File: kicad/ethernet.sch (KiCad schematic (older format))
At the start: 5 parts

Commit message: add ksz9021gn, cfps-73 to library
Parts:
- removed D? (x2): 88e1512, symbol 88e1512
- added D?: KSZ9021GN, symbol KSZ9021GN
- added D? (x3): 10cl025, symbol 10cl025
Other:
- moved on the sheet: D?, X?
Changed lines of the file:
@@
 LIBS:contrib
 LIBS:valves
-LIBS:88e1512
 LIBS:10cl025
 LIBS:l829-1j1t-43
 LIBS:nup4114upxv6t1g
+LIBS:ksz9021rl
+LIBS:ksz9021gn
+LIBS:cfps-73
+LIBS:fpgagigepi-cache
 EELAYER 25 0
 EELAYER END
@@
 encoding utf-8
 Sheet 3 4
-Title ""
-Date ""
-Rev ""
-Comp ""
-Comment1 ""
-Comment2 ""
+Title "figa-pi"
+Date "2018-04-13"
+Rev "1.0"
+Comp "GENERAL RND"
+Comment1 "07e20003"
+Comment2 "Y. Remizov"
 Comment3 ""
 Comment4 ""
@@
 L L829-1J1T-43 X?
 U 1 1 5AC780DA
-P 9200 2400
-F 0 "X?" H 8700 3250 60  0000 C CNN
-F 1 "L829-1J1T-43" H 9450 3250 60  0000 C CNN
-F 2 "" H 9200 2700 60  0001 C CNN
-F 3 "" H 9200 2700 60  0001 C CNN
-	1    9200 2400
-	1    0    0    -1
-$EndComp
-$Comp
-L 88e1512 D?
-U 1 1 5AC7812F
-P 5400 2500
-F 0 "D?" H 4500 3550 60  0000 C CNN
-F 1 "88e1512" H 5400 3100 60  0000 C CNN
-F 2 "" H 5350 2600 60  0001 C CNN
-F 3 "" H 5350 2600 60  0001 C CNN
-	1    5400 2500
-	1    0    0    -1
-$EndComp
-$Comp
-L 88e1512 D?
-U 2 1 5AC78188
-P 5350 5200
-F 0 "D?" H 4450 6250 60  0000 C CNN
-F 1 "88e1512" H 5350 5800 60  0000 C CNN
-F 2 "" H 5300 5300 60  0001 C CNN
-F 3 "" H 5300 5300 60  0001 C CNN
-	2    5350 5200
+P 9200 2300
+F 0 "X?" H 8700 3150 60  0000 C CNN
+F 1 "L829-1J1T-43" H 9450 3150 60  0000 C CNN
+F 2 "" H 9200 2600 60  0001 C CNN
+F 3 "" H 9200 2600 60  0001 C CNN
+	1    9200 2300
 	1    0    0    -1
 $EndComp
@@
 L NUP4114UPXV6T1G D?
 U 1 1 5AC781CD
-P 8800 4300
-F 0 "D?" H 8600 4600 60  0000 C CNN
-F 1 "NUP4114UPXV6T1G" H 8800 4000 60  0000 C CNN
-F 2 "" H 8800 4250 60  0001 C CNN
-F 3 "" H 8800 4250 60  0001 C CNN
-	1    8800 4300
+P 8850 4050
+F 0 "D?" H 8650 4350 60  0000 C CNN
+F 1 "NUP4114UPXV6T1G" H 8850 3750 60  0000 C CNN
+F 2 "" H 8850 4000 60  0001 C CNN
+F 3 "" H 8850 4000 60  0001 C CNN
+	1    8850 4050
 	1    0    0    -1
 $EndComp
@@
 L NUP4114UPXV6T1G D?
 U 1 1 5AC78238
-P 8800 5200
-F 0 "D?" H 8600 5500 60  0000 C CNN
-F 1 "NUP4114UPXV6T1G" H 8800 4900 60  0000 C CNN
-F 2 "" H 8800 5150 60  0001 C CNN
-F 3 "" H 8800 5150 60  0001 C CNN
-	1    8800 5200
+P 8850 4950
+F 0 "D?" H 8650 5250 60  0000 C CNN
+F 1 "NUP4114UPXV6T1G" H 8850 4650 60  0000 C CNN
+F 2 "" H 8850 4900 60  0001 C CNN
+F 3 "" H 8850 4900 60  0001 C CNN
+	1    8850 4950
 	1    0    0    -1
 $EndComp
+$Comp
+L KSZ9021GN D?
+U 1 1 5AD094DF
+P 5500 3100
+F 0 "D?" H 4950 4750 60  0000 C CNN
+F 1 "KSZ9021GN" H 5850 4750 60  0000 C CNN
+F 2 "" H 5250 4000 60  0001 C CNN
+F 3 "" H 5250 4000 60  0001 C CNN
+	1    5500 3100
+	1    0    0    -1
+$EndComp
+$Comp
+L 10cl025 D?
+U 4 1 5AD09564
+P 1550 2100
+F 0 "D?" H 1200 2750 60  0000 C CNN
+F 1 "10cl025" H 1800 2750 60  0000 C CNN
+F 2 "" H 550 2450 60  0001 C CNN
+F 3 "" H 550 2450 60  0001 C CNN
+	4    1550 2100
+	-1   0    0    -1
+$EndComp
+$Comp
+L 10cl025 D?
+U 7 1 5AD095B3
+P 1550 3600
+F 0 "D?" H 1200 4250 60  0000 C CNN
+F 1 "10cl025" H 1800 4250 60  0000 C CNN
+F 2 "" H 550 3950 60  0001 C CNN
+F 3 "" H 550 3950 60  0001 C CNN
+	7    1550 3600
+	-1   0    0    -1
+$EndComp
+$Comp
+L 10cl025 D?
+U 8 1 5AD09652
+P 1550 5000
+F 0 "D?" H 1200 5650 60  0000 C CNN
+F 1 "10cl025" H 1800 5650 60  0000 C CNN
+F 2 "" H 550 5350 60  0001 C CNN
+F 3 "" H 550 5350 60  0001 C CNN
+	8    1550 5000
+	-1   0    0    -1
+$EndComp
 $EndSCHEMATC

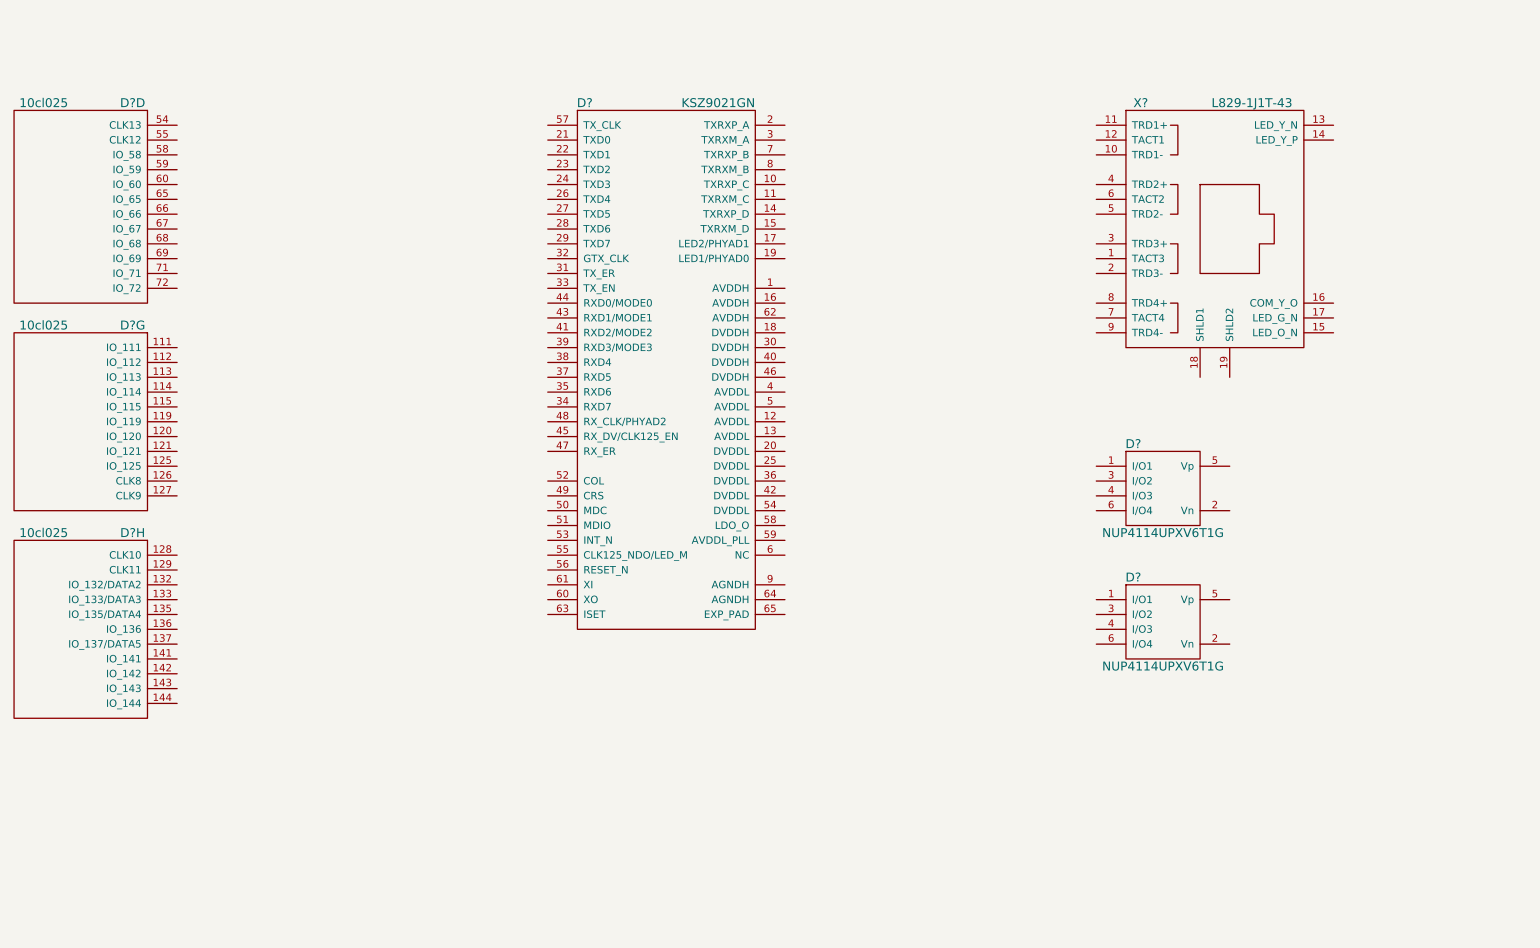
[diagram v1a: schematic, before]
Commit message: add tlv62080 to library, continue design schematic
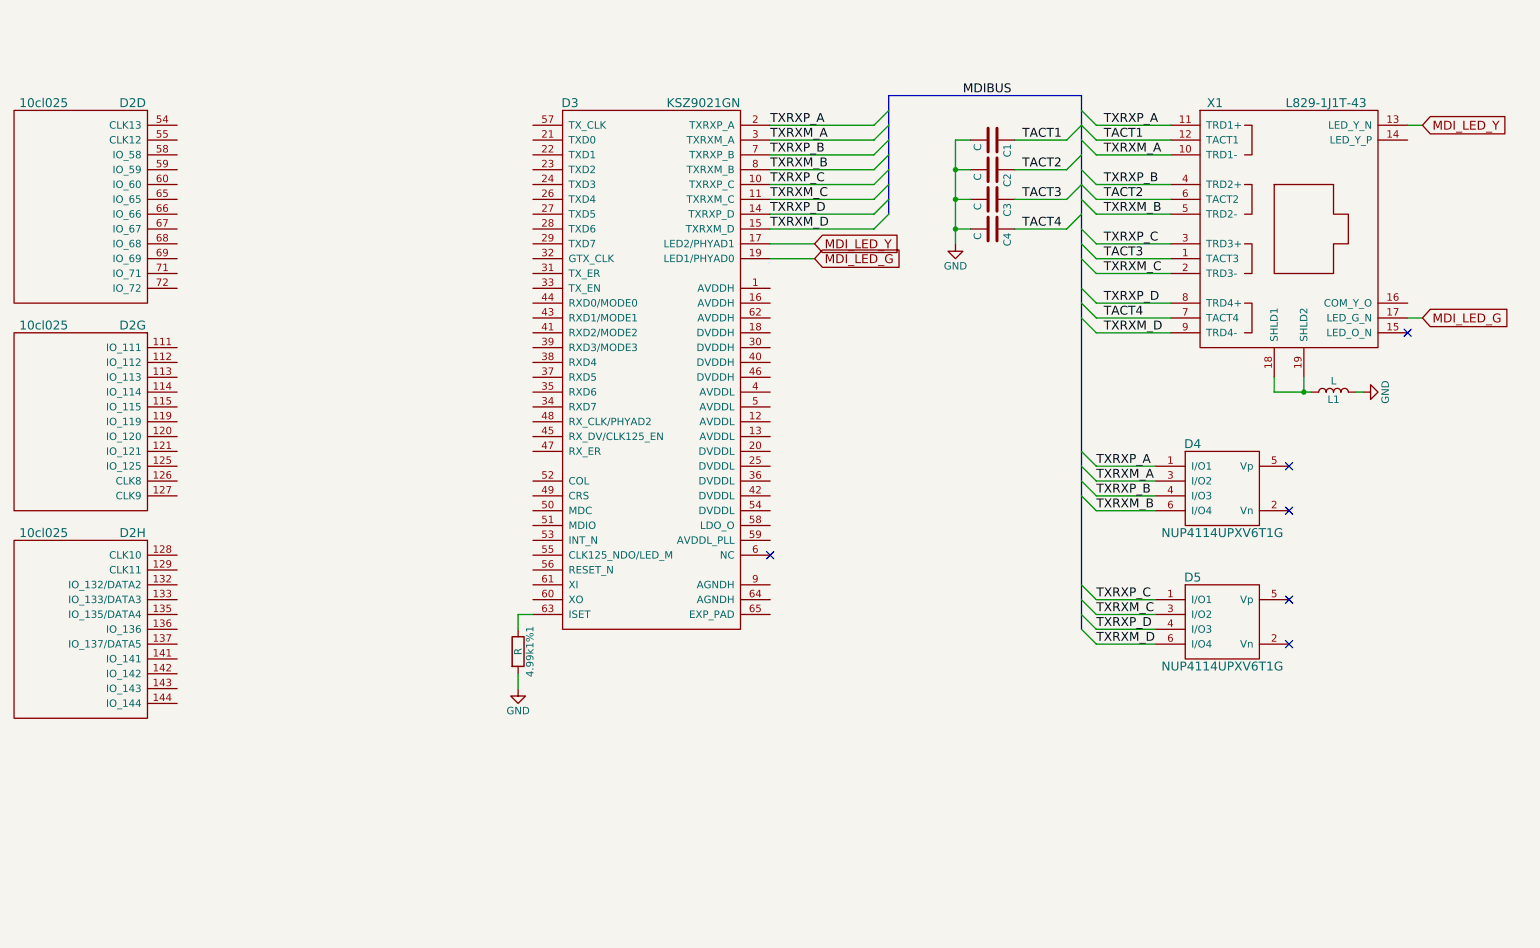
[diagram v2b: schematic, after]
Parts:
- added 4.99k1%1: R, symbol R
- added C1, C2, C3, C4: C, symbol C
- added L1: L, symbol L
- gave numbers to parts that had none: 5
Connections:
- net TACT3: now reaches X1.1 (TACT3)
- net TACT3: now also C3.1
- net TXRXM_A: now reaches X1.10 (TRD1-)
- net TXRXM_A: now also D3.3 (TXRXM_A), D4.3 (I/O2)
- net TXRXP_A: now reaches X1.11 (TRD1+)
- net TXRXP_A: now also D3.2 (TXRXP_A), D4.1 (I/O1)
- net TACT1: now reaches X1.12 (TACT1)
- net TACT1: now also C1.1
- net MDI_LED_Y: now reaches X1.13 (LED_Y_N)
- net MDI_LED_Y: now also D3.17 (LED2/PHYAD1)
- net MDI_LED_G: now reaches X1.17 (LED_G_N)
- net MDI_LED_G: now also D3.19 (LED1/PHYAD0)
- net at X1.18 (SHLD1): now also X1.19 (SHLD2), L1.1
- net TXRXM_C: now reaches X1.2 (TRD3-)
- net TXRXM_C: now also D3.11 (TXRXM_C), D5.3 (I/O2)
- net TXRXP_C: now reaches X1.3 (TRD3+)
- net TXRXP_C: now also D3.10 (TXRXP_C), D5.1 (I/O1)
- net TXRXP_B: now reaches X1.4 (TRD2+)
- net TXRXP_B: now also D3.7 (TXRXP_B), D4.4 (I/O3)
- net TXRXM_B: now reaches X1.5 (TRD2-)
- net TXRXM_B: now also D3.8 (TXRXM_B), D4.6 (I/O4)
- net TACT2: now reaches X1.6 (TACT2)
- net TACT2: now also C2.1
- net TACT4: now reaches X1.7 (TACT4)
- net TACT4: now also C4.1
- net TXRXP_D: now reaches X1.8 (TRD4+)
- net TXRXP_D: now also D3.14 (TXRXP_D), D5.4 (I/O3)
- net TXRXM_D: now reaches X1.9 (TRD4-)
- net TXRXM_D: now also D3.15 (TXRXM_D), D5.6 (I/O4)
- net at D3.63 (ISET): now also 4.99k1%1.1
- new net GND: 4.99k1%1.2, C1.2, C2.2, C3.2, C4.2, L1.2
- no-connect marks 0 -> 6
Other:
- moved on the sheet: D3, D4, D5, X1

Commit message: add nb3l553dr2g to library, continue design schematic
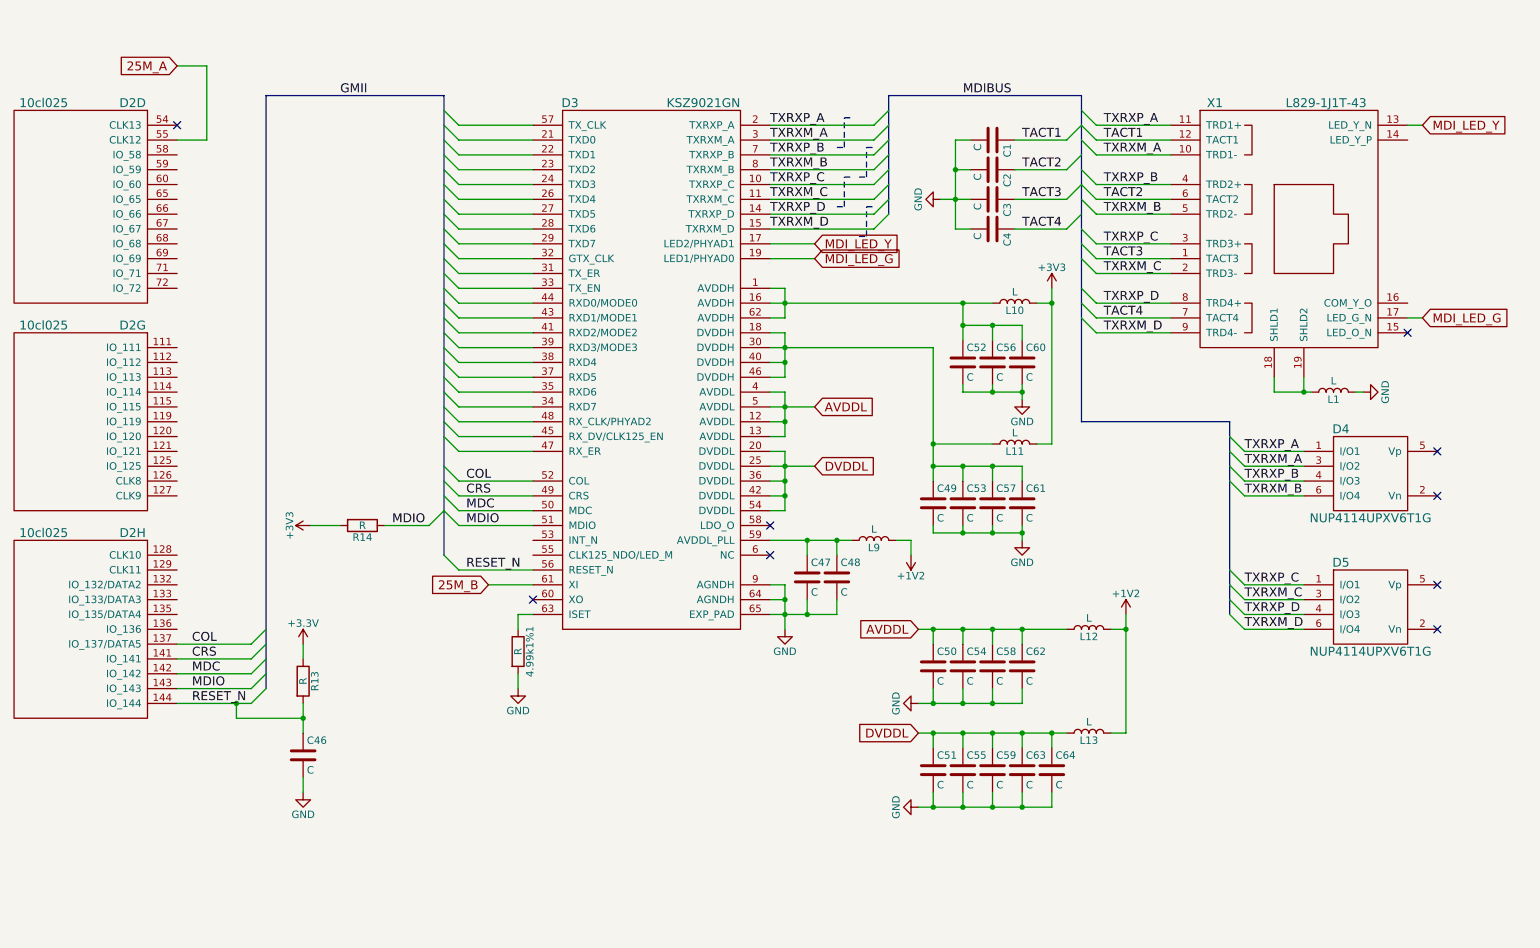
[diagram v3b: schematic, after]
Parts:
- added C46, C47, C48, C49, C50, C51, C52, C53, C54, C55, C56, C57, C58, C59, C60, C61, C62, C63, C64: C, symbol C
- added L10, L11, L12, L13, L9: L, symbol L
- added R13, R14: R, symbol R
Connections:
- net GND: now also D3.64 (AGNDH), D3.65 (EXP_PAD), D3.9 (AGNDH), C46.2, C47.2, C48.2, C49.2, C50.2, C51.2, C52.2, C53.2, C54.2, C55.2, C56.2, C57.2, C58.2, C59.2, C60.2, C61.2, C62.2, C63.2, C64.2
- net at D3.1 (AVDDH): now also D3.16 (AVDDH), D3.62 (AVDDH), C52.1, C56.1, C60.1, L10.1
- net AVDDL: now reaches D3.12 (AVDDL)
- net AVDDL: now also D3.13 (AVDDL), D3.4 (AVDDL), D3.5 (AVDDL), C50.1, C54.1, C58.1, C62.1, L12.1
- net at D3.18 (DVDDH): now also D3.30 (DVDDH), D3.40 (DVDDH), D3.46 (DVDDH), C49.1, C53.1, C57.1, C61.1, L11.1
- net DVDDL: now reaches D3.20 (DVDDL)
- net DVDDL: now also D3.25 (DVDDL), D3.36 (DVDDL), D3.42 (DVDDL), D3.54 (DVDDL), C51.1, C55.1, C59.1, C63.1, C64.1, L13.1
- net CRS: now reaches D3.49 (CRS)
- net CRS: now also D2.141 (IO_141)
- net MDC: now reaches D3.50 (MDC)
- net MDC: now also D2.142 (IO_142)
- net MDIO: now reaches D3.51 (MDIO)
- net MDIO: now also D2.143 (IO_143), R14.1
- net COL: now reaches D3.52 (COL)
- net COL: now also D2.137 (IO_137/DATA5)
- net RESET_N: now reaches D3.56 (RESET_N)
- net RESET_N: now also D2.144 (IO_144), C46.1, R13.2
- net at D3.59 (AVDDL_PLL): now also C47.1, C48.1, L9.1
- net 25M_B: now reaches D3.61 (XI)
- net 25M_A: now reaches D2.55 (CLK12)
- new net +1V2: L12.2, L13.2, L9.2
- new net +3V3: L10.2, L11.2, R13.1, R14.2
- no-connect marks 6 -> 9
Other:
- moved on the sheet: D4, D5

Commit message: continue design schematic
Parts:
- removed D4, D5: NUP4114UPXV6T1G, symbol NUP4114UPXV6T1G
- added U2, U3: NUP4114UPXV6T1G, symbol NUP4114UPXV6T1G
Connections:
- net GND: now also D2.126 (CLK8), D2.127 (CLK9), D2.128 (CLK10), D2.129 (CLK11), D2.54 (CLK13)
- net TXRXM_A: now also U2.3 (I/O2)
- net TXRXM_B: now also U2.6 (I/O4)
- net TXRXM_C: now also U3.3 (I/O2)
- net TXRXM_D: now also U3.6 (I/O4)
- net TXRXP_A: now also U2.1 (I/O1)
- net TXRXP_B: now also U2.4 (I/O3)
- net TXRXP_C: now also U3.1 (I/O1)
- net TXRXP_D: now also U3.4 (I/O3)
- net TXD0: now reaches D3.21 (TXD0)
- net TXD0: now also D2.58 (IO_58)
- net TXD1: now reaches D3.22 (TXD1)
- net TXD1: now also D2.59 (IO_59)
- net TXD2: now reaches D3.23 (TXD2)
- net TXD2: now also D2.60 (IO_60)
- net TXD3: now reaches D3.24 (TXD3)
- net TXD3: now also D2.65 (IO_65)
- net TXD4: now reaches D3.26 (TXD4)
- net TXD4: now also D2.66 (IO_66)
- net TXD5: now reaches D3.27 (TXD5)
- net TXD5: now also D2.67 (IO_67)
- net TXD6: now reaches D3.28 (TXD6)
- net TXD6: now also D2.68 (IO_68)
- net TXD7: now reaches D3.29 (TXD7)
- net TXD7: now also D2.69 (IO_69)
- net TX_ER: now reaches D3.31 (TX_ER)
- net TX_ER: now also D2.132 (IO_132/DATA2)
- net GTX_CLK: now reaches D3.32 (GTX_CLK)
- net GTX_CLK: now also D2.72 (IO_72)
- net TX_EN: now reaches D3.33 (TX_EN)
- net TX_EN: now also D2.133 (IO_133/DATA3)
- net RXD7: now reaches D3.34 (RXD7)
- net RXD7: now also D2.121 (IO_121)
- net RXD6: now reaches D3.35 (RXD6)
- net RXD6: now also D2.120 (IO_120)
- net RXD5: now reaches D3.37 (RXD5)
- net RXD5: now also D2.119 (IO_119)
- net RXD4: now reaches D3.38 (RXD4)
- net RXD4: now also D2.115 (IO_115)
- net RXD3: now reaches D3.39 (RXD3/MODE3)
- net RXD3: now also D2.114 (IO_114)
- net RXD2: now reaches D3.41 (RXD2/MODE2)
- net RXD2: now also D2.113 (IO_113)
- net RXD1: now reaches D3.43 (RXD1/MODE1)
- net RXD1: now also D2.112 (IO_112)
- net RXD0: now reaches D3.44 (RXD0/MODE0)
- net RXD0: now also D2.111 (IO_111)
- net RX_DV: now reaches D3.45 (RX_DV/CLK125_EN)
- net RX_DV: now also D2.135 (IO_135/DATA4)
- net RX_ER: now reaches D3.47 (RX_ER)
- net RX_ER: now also D2.136 (IO_136)
- net RX_CLK: now reaches D3.48 (RX_CLK/PHYAD2)
- net RX_CLK: now also D2.125 (IO_125)
- net TX_CLK: now reaches D3.57 (TX_CLK)
- net TX_CLK: now also D2.71 (IO_71)
- no-connect marks 9 -> 8
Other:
- note added: "TODO \n-check pullup/pulldown\n-mode set\n-leds resistors\n-leds resitors"
